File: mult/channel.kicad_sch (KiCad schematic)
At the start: 15 parts, among them J2 Eurorack_Mono_Jack, J3 Eurorack_Mono_Jack, J4 Eurorack_Mono_Jack, J5 Eurorack_Mono_Jack, U1 OPA4197xPW

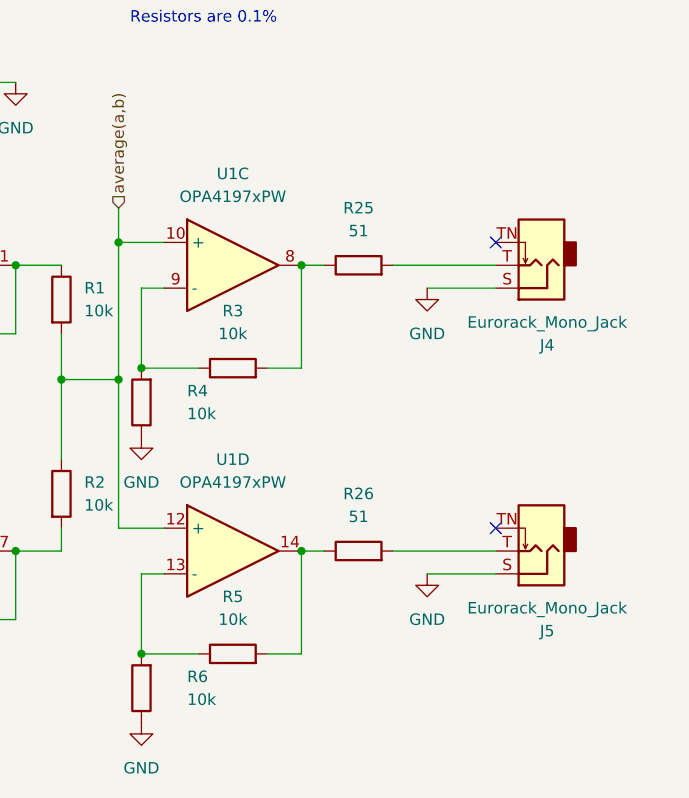
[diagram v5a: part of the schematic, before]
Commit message: mult: Misc partial progress
At least since last commit:

* New LEDs (no dual unit)
* Jack placement, share sleeve pin
* Board fit within 20x108mm
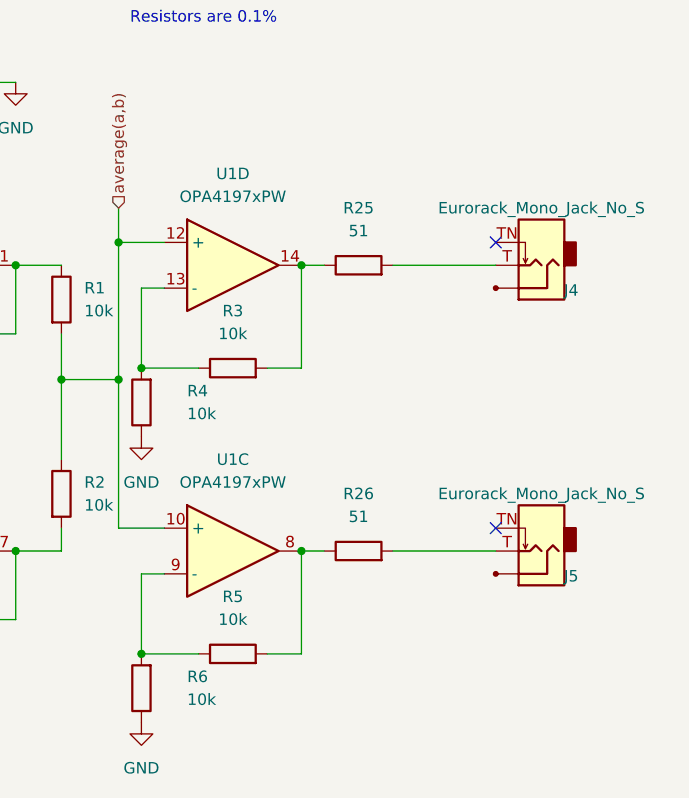
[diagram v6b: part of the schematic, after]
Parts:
- C3, C4: footprint Capacitor_SMD:C_0805_2012Metric -> Capacitor_SMD:C_0805_2012Metric_Pad1.18x1.45mm_HandSolder
- J2, J3: footprint winterbloom:AudioJack_WQP518MA -> winterbloom:AudioJack_WQP518MA_Compact_S
- J4, J5: value Eurorack_Mono_Jack -> Eurorack_Mono_Jack_No_S; footprint winterbloom:AudioJack_WQP518MA -> winterbloom:AudioJack_WQP518MA_No_S; symbol winterbloom:Eurorack_Mono_Jack -> winterbloom:Eurorack_Mono_Jack_No_S
- R1, R2, R25, R26, R3, R4, R5, R6: footprint Resistor_SMD:R_0805_2012Metric -> Resistor_SMD:R_0805_2012Metric_Pad1.20x1.40mm_HandSolder
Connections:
- net GND: no longer J4.S (Sleeve), J5.S (Sleeve)
- net average(a,b): now also U1.10 (+), U1.12 (+); no longer U1.10 (+), U1.12 (+)
- net at R25.1, R3.2: now also U1.14; no longer U1.8
- net at R3.1, R4.2: now also U1.13 (-); no longer U1.9 (-)
- net at R5.1, R6.2: now also U1.9 (-); no longer U1.13 (-)
- net at R26.1, R5.2: now also U1.8; no longer U1.14
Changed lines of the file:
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@@
-    (stroke (width 0) (type default))
-  )
-  (wire (pts (xy 137.16 63.5) (xy 144.78 63.5))
     (stroke (width 0) (type default))
   )
   (wire (pts (xy 125.73 60.96) (xy 123.19 60.96))
-    (stroke (width 0) (type default))
-  )
-  (wire (pts (xy 137.16 95.25) (xy 144.78 95.25))
     (stroke (width 0) (type default))
   )
@@
       (effects (font (size 1.27 1.27)))
     )
-    (property "Footprint" "Capacitor_SMD:C_0805_2012Metric" (at 88.9 39.6748 0)
+    (property "Footprint" "Capacitor_SMD:C_0805_2012Metric_Pad1.18x1.45mm_HandSolder" (at 88.9 39.6748 0)
       (effects (font (size 1.27 1.27)) hide)
     )
@@
       (effects (font (size 1.27 1.27)))
     )
-    (property "Footprint" "winterbloom:AudioJack_WQP518MA" (at 55.88 97.79 0)
+    (property "Footprint" "winterbloom:AudioJack_WQP518MA_Compact_S" (at 55.88 97.79 0)
       (effects (font (size 1.27 1.27)) hide)
     )
@@
     )
   )
-  (symbol (lib_id "Amplifier_Operational:OPA4197xPW") (at 115.57 60.96 0) (unit 3)
+  (symbol (lib_id "Amplifier_Operational:OPA4197xPW") (at 115.57 60.96 0) (unit 4)
     (in_bom yes) (on_board yes) (dnp no) (fields_autoplaced)
     (property "Reference" "U1" (at 115.57 50.8 0)
@@
       (project "mult"
         (path "/0e98ec4b-b4c7-447c-abd7-a761177a7f67/2249c80e-b931-4fee-ab04-d512ceb5f269"
-          (reference "U1") (unit 3)
+          (reference "U1") (unit 4)
         )
         (path "/0e98ec4b-b4c7-447c-abd7-a761177a7f67/b290c7a8-131c-4f39-ab4f-62063cf2647f"
@@
         (path "/0e98ec4b-b4c7-447c-abd7-a761177a7f67/c8627544-d82d-426a-84eb-b4928bf7d17c"
           (reference "U4") (unit 3)
-        )
-      )
-    )
-  )
-  (symbol (lib_id "power:GND") (at 137.16 95.25 0) (unit 1)
-    (in_bom yes) (on_board yes) (dnp no) (fields_autoplaced)
-    (property "Reference" "#PWR07" (at 137.16 101.6 0)
-      (effects (font (size 1.27 1.27)) hide)
-    )
-    (property "Value" "GND" (at 137.16 100.33 0)
-      (effects (font (size 1.27 1.27)))
-    )
-    (property "Footprint" "" (at 137.16 95.25 0)
-      (effects (font (size 1.27 1.27)) hide)
-    )
-    (property "Datasheet" "" (at 137.16 95.25 0)
-      (effects (font (size 1.27 1.27)) hide)
-    )
-    (pin "1")
-    (instances
-      (project "mult"
-        (path "/0e98ec4b-b4c7-447c-abd7-a761177a7f67/2249c80e-b931-4fee-ab04-d512ceb5f269"
-          (reference "#PWR07") (unit 1)
-        )
-        (path "/0e98ec4b-b4c7-447c-abd7-a761177a7f67/b290c7a8-131c-4f39-ab4f-62063cf2647f"
-          (reference "#PWR020") (unit 1)
-        )
-        (path "/0e98ec4b-b4c7-447c-abd7-a761177a7f67/b26d7339-1ce2-4103-8db8-9f6dbd3f09ef"
-          (reference "#PWR028") (unit 1)
-        )
-        (path "/0e98ec4b-b4c7-447c-abd7-a761177a7f67/c8627544-d82d-426a-84eb-b4928bf7d17c"
-          (reference "#PWR038") (unit 1)
         )
       )
@@
       (effects (font (size 1.27 1.27)) (justify left))
     )
-    (property "Footprint" "Resistor_SMD:R_0805_2012Metric" (at 94.742 86.36 90)
+    (property "Footprint" "Resistor_SMD:R_0805_2012Metric_Pad1.20x1.40mm_HandSolder" (at 94.742 86.36 90)
       (effects (font (size 1.27 1.27)) hide)
     )
@@
       (effects (font (size 1.27 1.27)))
     )
-    (property "Footprint" "winterbloom:AudioJack_WQP518MA" (at 55.88 66.04 0)
+    (property "Footprint" "winterbloom:AudioJack_WQP518MA_Compact_S" (at 55.88 66.04 0)
       (effects (font (size 1.27 1.27)) hide)
     )
@@
       (effects (font (size 1.27 1.27)))
     )
-    (property "Footprint" "Resistor_SMD:R_0805_2012Metric" (at 129.54 62.738 90)
+    (property "Footprint" "Resistor_SMD:R_0805_2012Metric_Pad1.20x1.40mm_HandSolder" (at 129.54 62.738 90)
       (effects (font (size 1.27 1.27)) hide)
     )
@@
       (effects (font (size 1.27 1.27)) (justify left))
     )
-    (property "Footprint" "Resistor_SMD:R_0805_2012Metric" (at 94.742 64.77 90)
+    (property "Footprint" "Resistor_SMD:R_0805_2012Metric_Pad1.20x1.40mm_HandSolder" (at 94.742 64.77 90)
       (effects (font (size 1.27 1.27)) hide)
     )
@@
       (effects (font (size 1.27 1.27)) (justify right))
     )
-    (property "Footprint" "Resistor_SMD:R_0805_2012Metric" (at 107.188 76.2 90)
+    (property "Footprint" "Resistor_SMD:R_0805_2012Metric_Pad1.20x1.40mm_HandSolder" (at 107.188 76.2 90)
       (effects (font (size 1.27 1.27)) hide)
     )
@@
     )
   )
-  (symbol (lib_id "Amplifier_Operational:OPA4197xPW") (at 115.57 92.71 0) (unit 4)
+  (symbol (lib_id "Amplifier_Operational:OPA4197xPW") (at 115.57 92.71 0) (unit 3)
     (in_bom yes) (on_board yes) (dnp no) (fields_autoplaced)
     (property "Reference" "U1" (at 115.57 82.55 0)
@@
       (project "mult"
         (path "/0e98ec4b-b4c7-447c-abd7-a761177a7f67/2249c80e-b931-4fee-ab04-d512ceb5f269"
-          (reference "U1") (unit 4)
+          (reference "U1") (unit 3)
         )
         (path "/0e98ec4b-b4c7-447c-abd7-a761177a7f67/b290c7a8-131c-4f39-ab4f-62063cf2647f"
@@
     )
   )
-  (symbol (lib_id "winterbloom:Eurorack_Mono_Jack") (at 149.86 91.44 0) (unit 1)
+  (symbol (lib_id "winterbloom:Eurorack_Mono_Jack_No_S") (at 149.86 91.44 0) (unit 1)
     (in_bom yes) (on_board yes) (dnp no)
-    (property "Reference" "J5" (at 150.495 101.6 0)
-      (effects (font (size 1.27 1.27)))
-    )
-    (property "Value" "Eurorack_Mono_Jack" (at 150.495 99.06 0)
-      (effects (font (size 1.27 1.27)))
-    )
-    (property "Footprint" "winterbloom:AudioJack_WQP518MA" (at 151.13 100.33 0)
+    (property "Reference" "J5" (at 153.162 95.504 0)
+      (effects (font (size 1.27 1.27)))
+    )
+    (property "Value" "Eurorack_Mono_Jack_No_S" (at 149.86 86.36 0)
+      (effects (font (size 1.27 1.27)))
+    )
+    (property "Footprint" "winterbloom:AudioJack_WQP518MA_No_S" (at 151.13 100.33 0)
       (effects (font (size 1.27 1.27)) hide)
     )
@@
       (effects (font (size 1.27 1.27)) hide)
     )
-    (pin "S")
     (pin "T")
     (pin "TN")
@@
       (effects (font (size 1.27 1.27)))
     )
-    (property "Footprint" "Resistor_SMD:R_0805_2012Metric" (at 115.57 105.918 90)
+    (property "Footprint" "Resistor_SMD:R_0805_2012Metric_Pad1.20x1.40mm_HandSolder" (at 115.57 105.918 90)
       (effects (font (size 1.27 1.27)) hide)
     )
@@
       (effects (font (size 1.27 1.27)))
     )
-    (property "Footprint" "Capacitor_SMD:C_0805_2012Metric" (at 88.9 24.4348 0)
+    (property "Footprint" "Capacitor_SMD:C_0805_2012Metric_Pad1.18x1.45mm_HandSolder" (at 88.9 24.4348 0)
       (effects (font (size 1.27 1.27)) hide)
     )
@@
       (effects (font (size 1.27 1.27)))
     )
-    (property "Footprint" "Resistor_SMD:R_0805_2012Metric" (at 129.54 94.488 90)
+    (property "Footprint" "Resistor_SMD:R_0805_2012Metric_Pad1.20x1.40mm_HandSolder" (at 129.54 94.488 90)
       (effects (font (size 1.27 1.27)) hide)
     )
@@
         (path "/0e98ec4b-b4c7-447c-abd7-a761177a7f67/c8627544-d82d-426a-84eb-b4928bf7d17c"
           (reference "#PWR034") (unit 1)
-        )
-      )
-    )
-  )
-  (symbol (lib_id "power:GND") (at 137.16 63.5 0) (unit 1)
-    (in_bom yes) (on_board yes) (dnp no) (fields_autoplaced)
-    (property "Reference" "#PWR06" (at 137.16 69.85 0)
-      (effects (font (size 1.27 1.27)) hide)
-    )
-    (property "Value" "GND" (at 137.16 68.58 0)
-      (effects (font (size 1.27 1.27)))
-    )
-    (property "Footprint" "" (at 137.16 63.5 0)
-      (effects (font (size 1.27 1.27)) hide)
-    )
-    (property "Datasheet" "" (at 137.16 63.5 0)
-      (effects (font (size 1.27 1.27)) hide)
-    )
-    (pin "1")
-    (instances
-      (project "mult"
-        (path "/0e98ec4b-b4c7-447c-abd7-a761177a7f67/2249c80e-b931-4fee-ab04-d512ceb5f269"
-          (reference "#PWR06") (unit 1)
-        )
-        (path "/0e98ec4b-b4c7-447c-abd7-a761177a7f67/b290c7a8-131c-4f39-ab4f-62063cf2647f"
-          (reference "#PWR019") (unit 1)
-        )
-        (path "/0e98ec4b-b4c7-447c-abd7-a761177a7f67/b26d7339-1ce2-4103-8db8-9f6dbd3f09ef"
-          (reference "#PWR027") (unit 1)
-        )
-        (path "/0e98ec4b-b4c7-447c-abd7-a761177a7f67/c8627544-d82d-426a-84eb-b4928bf7d17c"
-          (reference "#PWR036") (unit 1)
         )
       )
@@
     )
   )
-  (symbol (lib_id "winterbloom:Eurorack_Mono_Jack") (at 149.86 59.69 0) (unit 1)
+  (symbol (lib_id "winterbloom:Eurorack_Mono_Jack_No_S") (at 149.86 59.69 0) (unit 1)
     (in_bom yes) (on_board yes) (dnp no)
-    (property "Reference" "J4" (at 150.495 69.85 0)
-      (effects (font (size 1.27 1.27)))
-    )
-    (property "Value" "Eurorack_Mono_Jack" (at 150.495 67.31 0)
-      (effects (font (size 1.27 1.27)))
-    )
-    (property "Footprint" "winterbloom:AudioJack_WQP518MA" (at 151.13 68.58 0)
+    (property "Reference" "J4" (at 153.162 63.754 0)
+      (effects (font (size 1.27 1.27)))
+    )
+    (property "Value" "Eurorack_Mono_Jack_No_S" (at 149.86 54.61 0)
+      (effects (font (size 1.27 1.27)))
+    )
+    (property "Footprint" "winterbloom:AudioJack_WQP518MA_No_S" (at 151.13 68.58 0)
       (effects (font (size 1.27 1.27)) hide)
     )
@@
       (effects (font (size 1.27 1.27)) hide)
     )
-    (pin "S")
     (pin "T")
     (pin "TN")
@@
       (effects (font (size 1.27 1.27)) (justify right))
     )
-    (property "Footprint" "Resistor_SMD:R_0805_2012Metric" (at 107.188 107.95 90)
+    (property "Footprint" "Resistor_SMD:R_0805_2012Metric_Pad1.20x1.40mm_HandSolder" (at 107.188 107.95 90)
       (effects (font (size 1.27 1.27)) hide)
     )
@@
       (effects (font (size 1.27 1.27)))
     )
-    (property "Footprint" "Resistor_SMD:R_0805_2012Metric" (at 115.57 74.168 90)
-      (effects (font (size 1.27 1.27)) hide)
-    )
+    (property "Footprint" "Resistor_SMD:R_0805_2012Metric_Pad1.20x1.40mm_HandSolder" (at 115.57 74.168 90)
+      (effects (font (size 1.27 1.27)) hide)
+    )

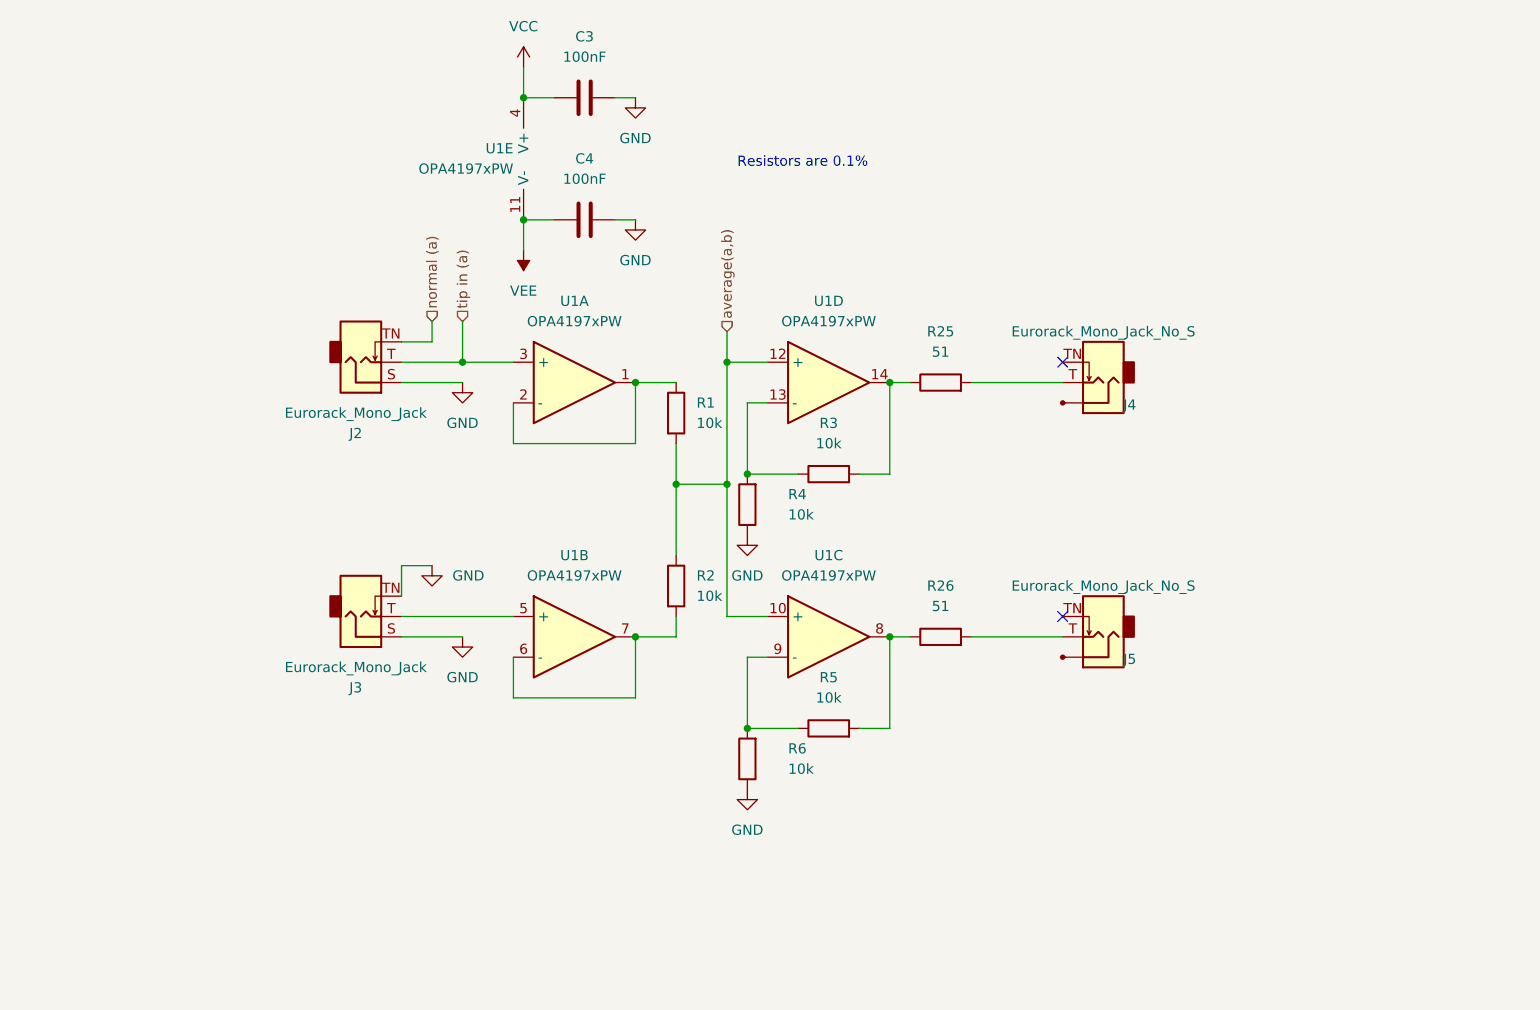
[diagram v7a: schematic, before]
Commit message: mult: Reorder channel schematic to match layout
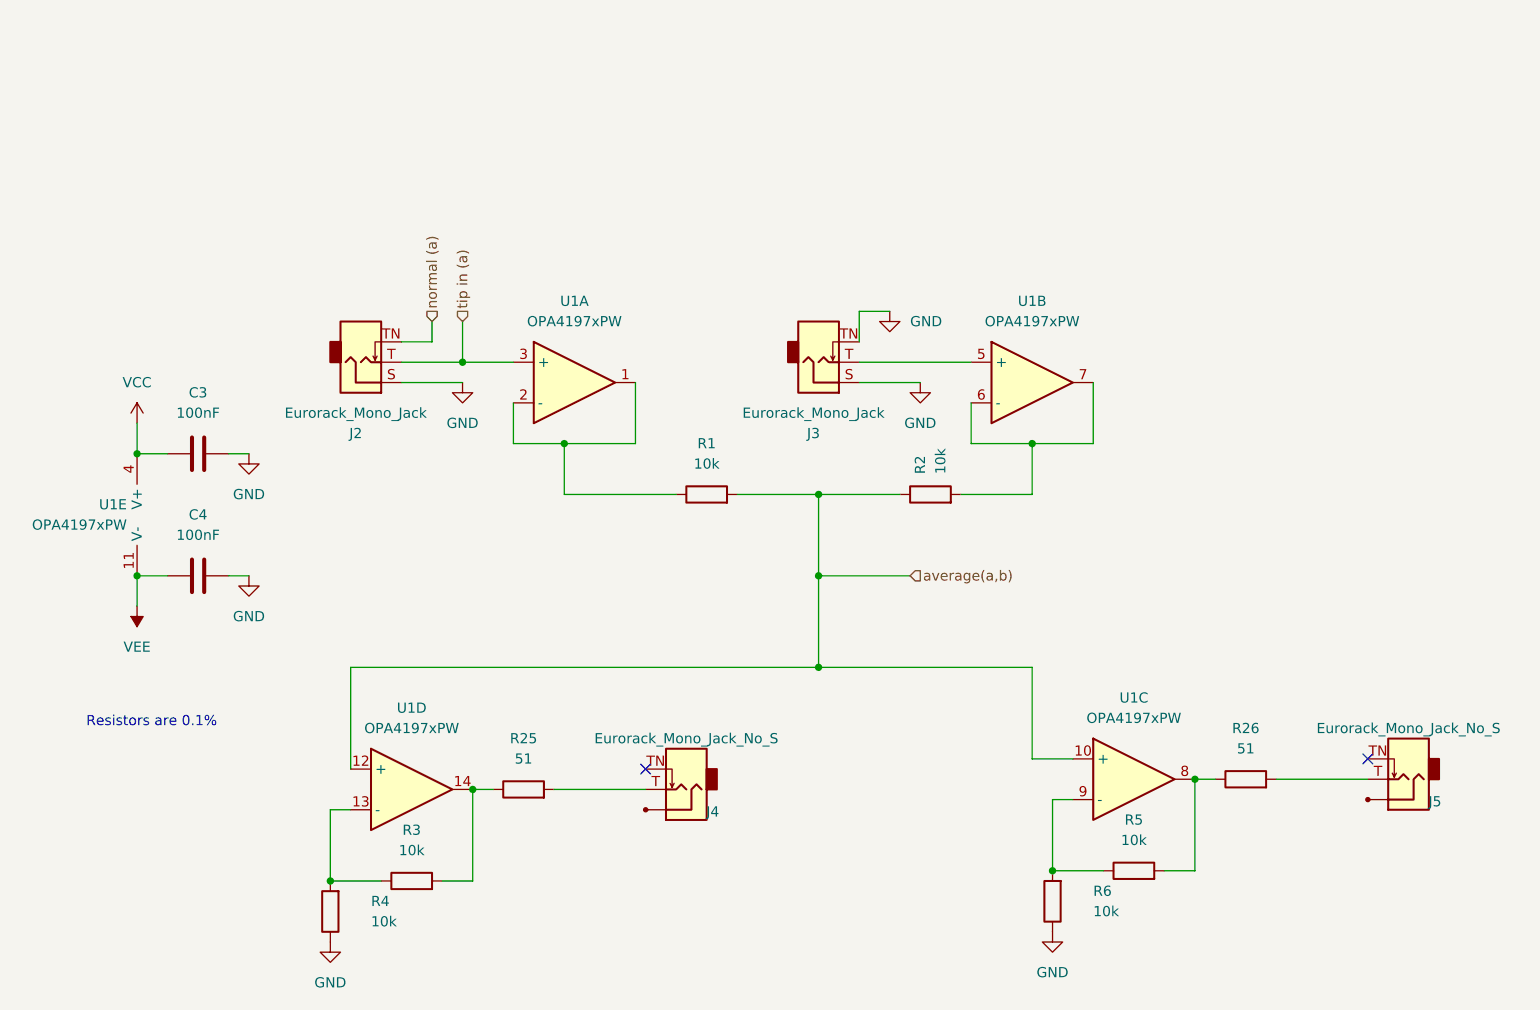
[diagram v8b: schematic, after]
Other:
- moved on the sheet: C3, C4, J3, J4, J5, R1, R2, R25, R26, R3, R4, R5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
